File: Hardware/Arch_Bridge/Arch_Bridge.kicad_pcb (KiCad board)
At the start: 2 copper layers, 88.8 x 76 mm, 87 parts, among them J1 Conn_01x02, J3 Conn_01x04, J4 Conn_01x04, Q1 2N3904, Q2 MJE2955, Q3 MJE2955, U1 AP63205WU, U10 74LVC1G04, U11 ESP32-S3-WROOM-1, U12 TXS0102DCT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

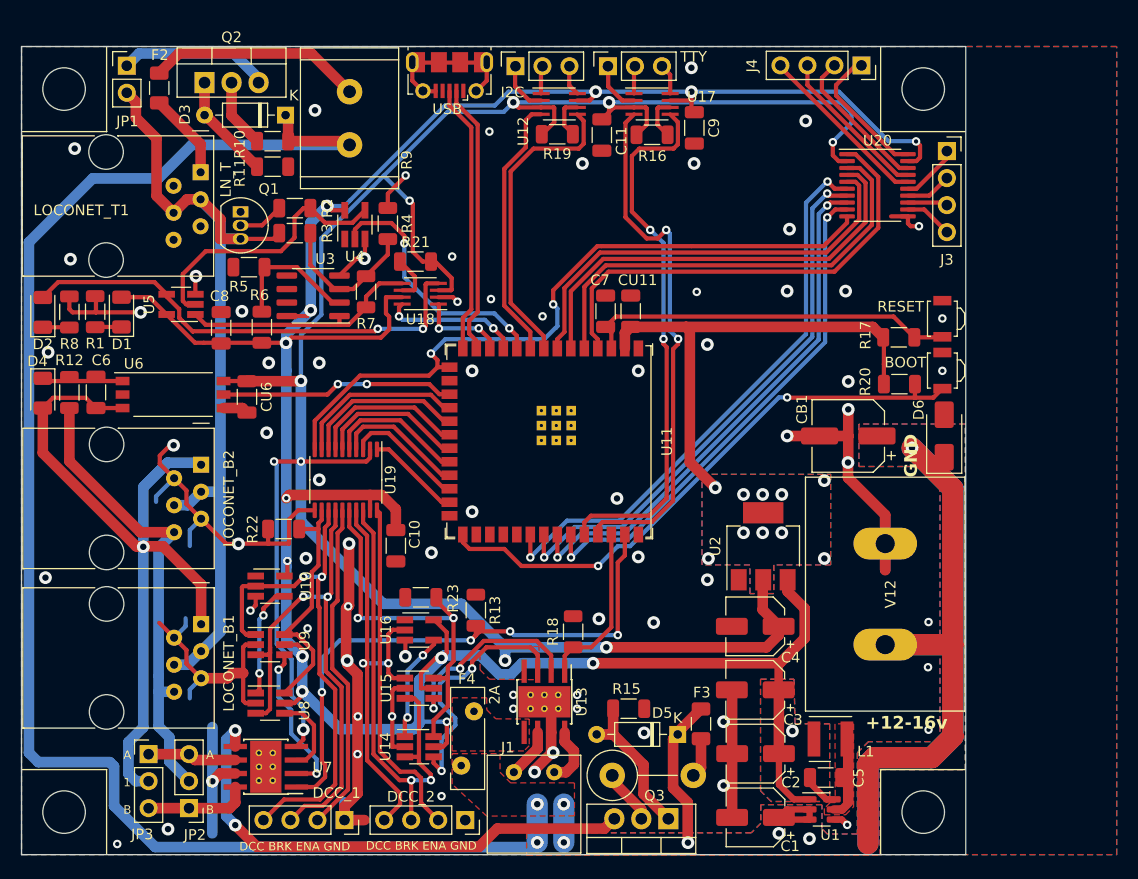
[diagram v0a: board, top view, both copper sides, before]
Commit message: Schematic rev 06 with PCB updates. Needs BOM and Fabs reprocessed.
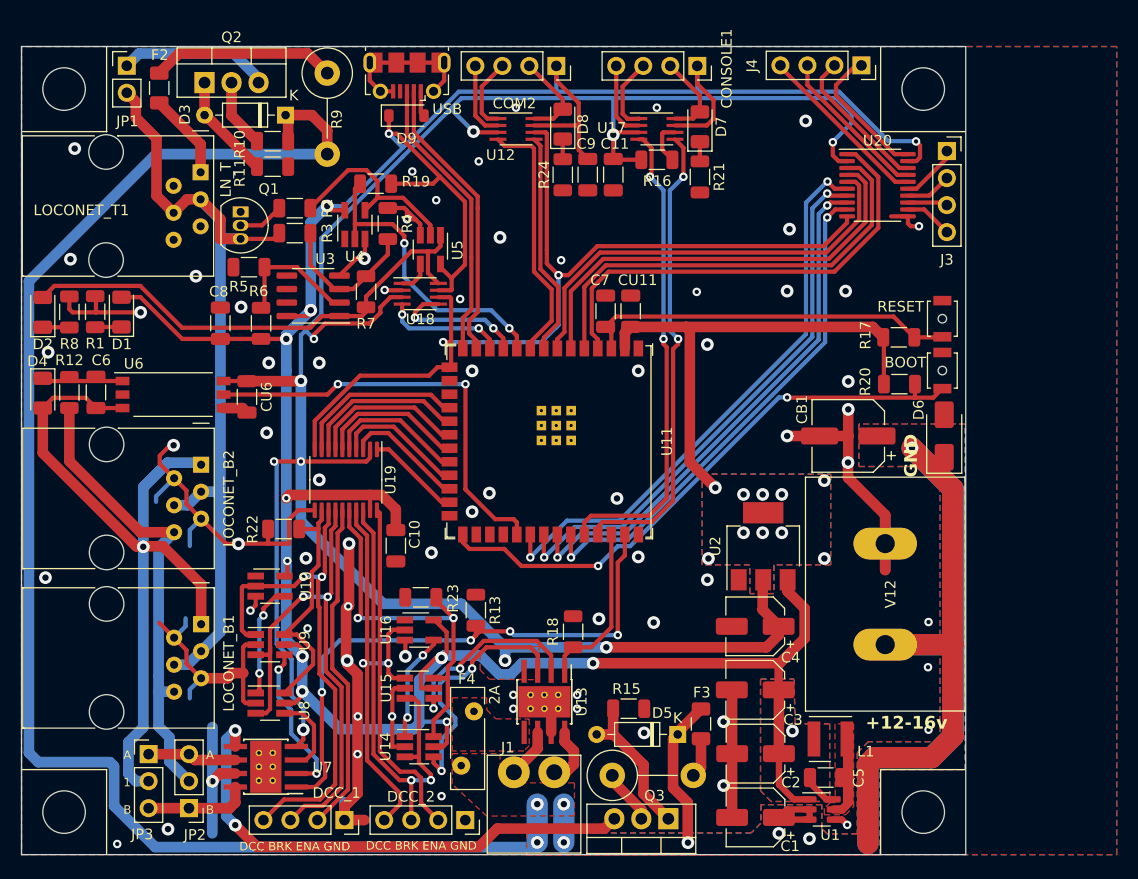
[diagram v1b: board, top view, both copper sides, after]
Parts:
- removed I2C_1, TTY_1: Conn_01x03, Connector_PinSocket_2.54mm:PinSocket_1x03_P2.54mm_Vertical
- added COM2: Conn_01x04, Connector_PinSocket_2.54mm:PinSocket_1x04_P2.54mm_Vertical, F.Cu at (70.3, 21.8)
- added CONSOLE1: Conn_01x03, Connector_PinSocket_2.54mm:PinSocket_1x04_P2.54mm_Vertical, F.Cu at (83.5, 21.8)
- added D7: LED, LED_SMD:LED_1206_3216Metric, F.Cu at (83.8, 27.6)
- added D8: LED, LED_SMD:LED_1206_3216Metric, F.Cu at (70.9, 27.3)
- added D9: PMEG2005EGW, Diode_SMD:D_SOD-123, F.Cu at (56.2, 26.5)
- added R24: 1k, Resistor_SMD:R_1206_3216Metric, F.Cu at (70.9, 32.1)
- BOOT1, RESET1: value B3U-3000P -> B3U-1000P; footprint Button_Switch_SMD:SW_SPST_B3U-3000P -> Button_Switch_SMD:SW_SPST_B3U-1000P-B
- F2: value 500mA -> 250mA
- R11: value 33k -> 3k
- R15: value 3k -> 470
- R21: value 10k -> 1k
- R22, R23: value 10k -> 47k
- R9: value 10 5w -> 33 2w; footprint Resistor_THT:R_Radial_Power_L13.0mm_W9.0mm_P5.00mm -> Resistor_THT:R_Axial_DIN0414_L11.9mm_D4.5mm_P7.62mm_Vertical
- moved R21 27.9 mm to (83.8, 32.3), turned to -90 degrees
- moved U5 24.0 mm to (58.5, 39.1), turned to -90 degrees
- moved R19 17.7 mm to (53.3, 32.9), turned to 0 degrees
- moved C9 10.9 mm to (73.2, 32.0)
- moved R9 7.07 mm to (48.8, 22.5), turned to -90 degrees
- moved U12 4.70 mm to (66.5, 27.8)
- moved USB1 4.00 mm to (56.2, 22.8)
- moved C11 3.88 mm to (75.7, 32.0)
- moved U17 2.39 mm to (79.8, 27.8)
- moved R16 2.39 mm to (79.8, 30.6)
- moved C8 0.43 mm to (38.7, 46.0)
- moved R6 0.37 mm to (42.5, 46.0)
- turned U18 to 0 degrees
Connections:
- R19 pad 1: Net-(U12-OE) -> /LN_TX
- R19 pad 2: +3.3V -> +5V
- R21 pad 1: +3.3V -> Net-(D7-K)
- R21 pad 2: Net-(U18-OE) -> GND
- R7 pad 1: Net-(U18-A1) -> Net-(D2-A)
- R9 pad 1: +12V -> Net-(F2-Pad2)
- R9 pad 2: Net-(F2-Pad2) -> +12V
- U11 pad 17: /RSYNC_IN -> /GPIO9
- U11 pad 31: /GPIO38 -> /RSYNC_IN
- U12 pad 6: Net-(U12-OE) -> /OE
- U17 pad 4: /TXD -> /RXD
- U17 pad 5: /RXD -> /TXD
- U18 pad 1: /LN_COLL -> Net-(U18-B2)
- U18 pad 4: Net-(D2-A) -> /LN_COLL
- U18 pad 5: Net-(U18-A1) -> /LN_RX
- U18 pad 6: Net-(U18-OE) -> /OE
- U18 pad 8: /LN_RX -> Net-(D2-A)
- U3 pad 1: Net-(U18-A1) -> Net-(D2-A)
- U5 pad 1: Net-(U18-A1) -> Net-(D2-A)
- U5 pad 4: Net-(D2-A) -> Net-(U18-B2)
- USB1 pad 1: unconnected-(USB1-VBUS-Pad1) -> Net-(D9-A)
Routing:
- net +5V: track 269.5 -> 306.3 mm, vias 14 -> 13
- net Net-(U18-A1): track 22.9 -> 0.00 mm
- net /OE: track 66.4 -> 87.0 mm
- net /RSYNC_IN: track 22.0 -> 40.3 mm
- net /SDA: track 28.9 -> 21.2 mm
- net Net-(R2-Pad2): track 25.7 -> 18.5 mm
- net /RXD: track 51.3 -> 45.0 mm
- net /TXD: track 49.9 -> 44.2 mm
- net Net-(COM2-Pin_2): track 2.84 -> 8.44 mm
- net Net-(CONSOLE1-Pin_2): track 2.84 -> 8.09 mm
- net Net-(CONSOLE1-Pin_3): track 2.57 -> 7.03 mm
- net Net-(U18-OE): track 4.43 -> 0.00 mm
- net Net-(COM2-Pin_3): track 2.57 -> 6.97 mm
- net /LN_TX: track 24.2 -> 28.5 mm
- net Net-(U12-OE): track 4.02 -> 0.00 mm
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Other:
- board text removed: "Arch Bridge Loconet interface + Railsync"
- board text removed: "I2C"
- board text removed: "TTY"

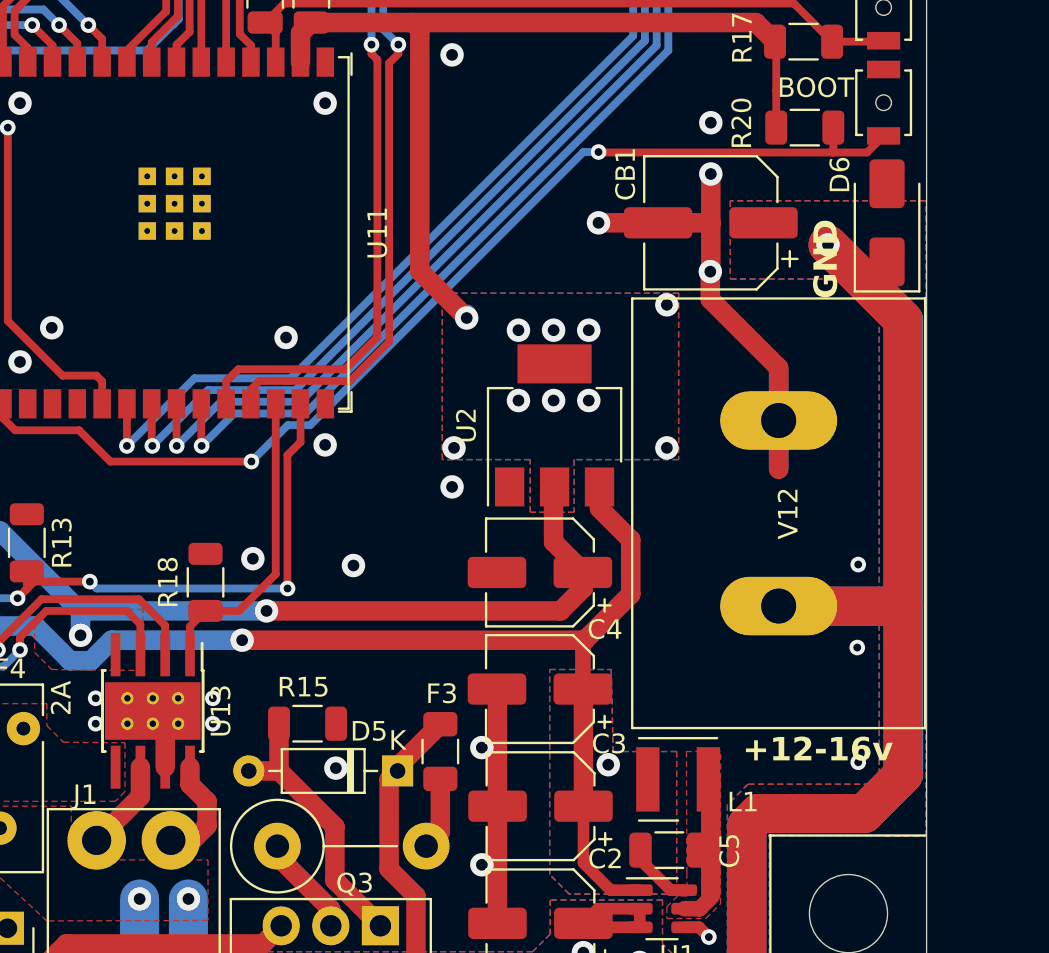
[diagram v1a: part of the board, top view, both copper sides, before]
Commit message: Changed CB1 to through hole for field installaion, no longer in BOM or populated by default.
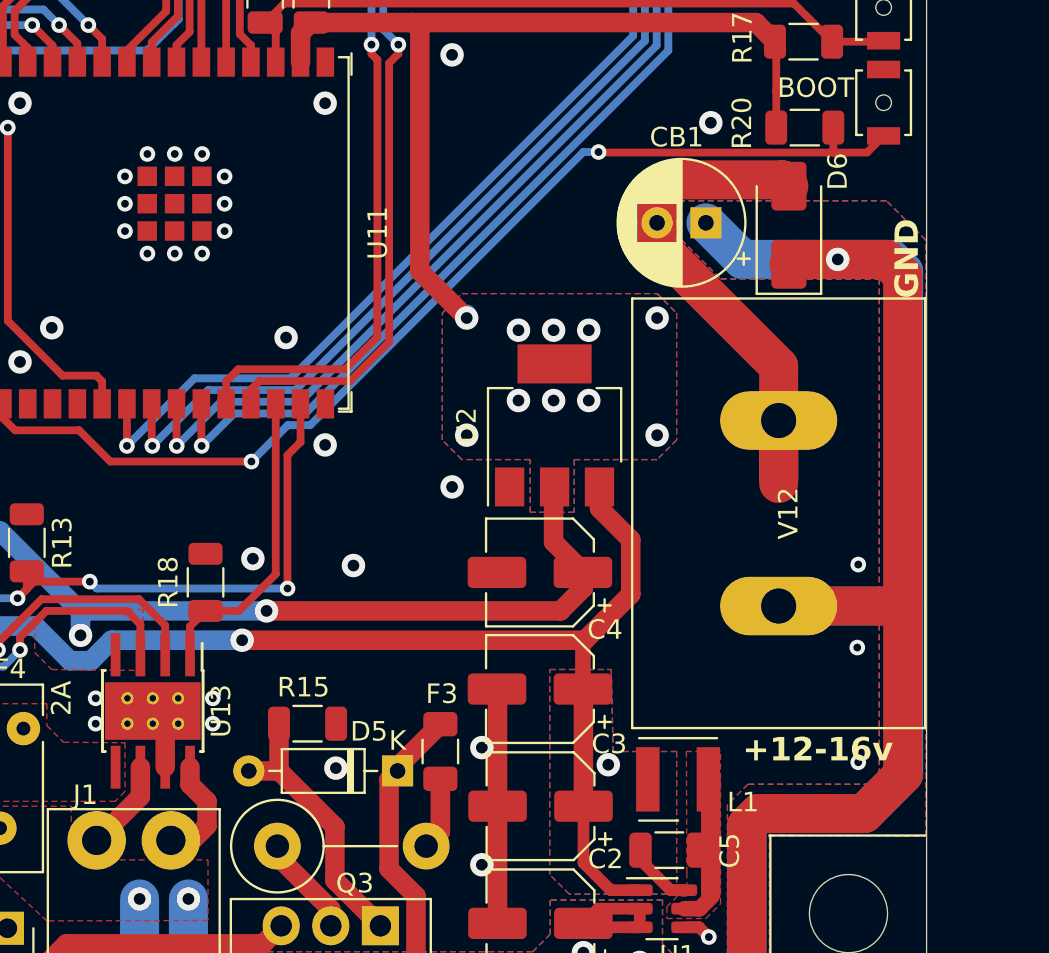
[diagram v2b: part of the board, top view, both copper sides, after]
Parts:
- CB1: footprint Capacitor_SMD:CP_Elec_6.3x7.7 -> Capacitor_THT:CP_Radial_D6.3mm_P2.50mm
- U5: value 74LVC1G02 -> 74xGxx_74AHC1G86
- moved D6 5.03 mm to (101.8, 56.8)
- moved CB1 0.25 mm to (97.5, 56.6)
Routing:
- net +12V: track 272.4 -> 283.7 mm
- net GND: track 209.3 -> 209.5 mm, vias 70 -> 79

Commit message: Added tags for JLCPCB Fabricaton
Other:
- board text added: "+"
- board text added: "-"
- board text added: "JLCJLCJLCJLC"
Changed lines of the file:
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@@
       (net 1 "GND") (pinfunction "GND") (pintype "passive"))
     (pad "41" smd rect (at -2.9 -1.94 90) (size 1 1) (layers "F.Cu" "F.Paste" "F.Mask")
-      (net 1 "GND") (pinfunction "GND") (pintype "passive") (zone_connect 2))
+      (net 1 "GND") (pinfunction "GND") (pintype "passive"))
     (pad "41" smd rect (at -2.9 -0.54 90) (size 1 1) (layers "F.Cu" "F.Paste" "F.Mask")
-      (net 1 "GND") (pinfunction "GND") (pintype "passive") (zone_connect 2))
+      (net 1 "GND") (pinfunction "GND") (pintype "passive"))
     (pad "41" smd rect (at -2.9 0.86 90) (size 1 1) (layers "F.Cu" "F.Paste" "F.Mask")
-      (net 1 "GND") (pinfunction "GND") (pintype "passive") (zone_connect 2))
+      (net 1 "GND") (pinfunction "GND") (pintype "passive"))
     (pad "41" smd rect (at -1.5 -1.94 90) (size 1 1) (layers "F.Cu" "F.Paste" "F.Mask")
-      (net 1 "GND") (pinfunction "GND") (pintype "passive") (zone_connect 2))
+      (net 1 "GND") (pinfunction "GND") (pintype "passive"))
     (pad "41" smd rect (at -1.5 -0.54 90) (size 1 1) (layers "F.Cu" "F.Paste" "F.Mask")
-      (net 1 "GND") (pinfunction "GND") (pintype "passive") (zone_connect 2))
+      (net 1 "GND") (pinfunction "GND") (pintype "passive"))
     (pad "41" smd rect (at -1.5 0.86 90) (size 1 1) (layers "F.Cu" "F.Paste" "F.Mask")
-      (net 1 "GND") (pinfunction "GND") (pintype "passive") (zone_connect 2))
+      (net 1 "GND") (pinfunction "GND") (pintype "passive"))
     (pad "41" smd rect (at -0.1 -1.94 90) (size 1 1) (layers "F.Cu" "F.Paste" "F.Mask")
-      (net 1 "GND") (pinfunction "GND") (pintype "passive") (zone_connect 2))
+      (net 1 "GND") (pinfunction "GND") (pintype "passive"))
     (pad "41" smd rect (at -0.1 -0.54 90) (size 1 1) (layers "F.Cu" "F.Paste" "F.Mask")
-      (net 1 "GND") (pinfunction "GND") (pintype "passive") (zone_connect 2))
+      (net 1 "GND") (pinfunction "GND") (pintype "passive"))
     (pad "41" smd rect (at -0.1 0.86 90) (size 1 1) (layers "F.Cu" "F.Paste" "F.Mask")
-      (net 1 "GND") (pinfunction "GND") (pintype "passive") (zone_connect 2))
+      (net 1 "GND") (pinfunction "GND") (pintype "passive"))
     (model "${ESPRESSIF_3DMODELS}/ESP32-S3-WROOM-1U.STEP"
       (offset (xyz -9 -9.75 0))
@@
   (gr_line (start 108.8 96) (end 108.8 20)
     (stroke (width 0.05) (type default)) (layer "Edge.Cuts"))
+  (gr_text "+" (at 98.5 79) (layer "B.SilkS")
+    (effects (font (size 1 1) (thickness 0.15)) (justify left bottom mirror))
+  )
+  (gr_text "JLCJLCJLCJLC" (at 108.25 66.75 90) (layer "B.SilkS")
+    (effects (font (size 1 1) (thickness 0.15)) (justify left bottom mirror))
+  )
+  (gr_text "-" (at 98.5 69.25) (layer "B.SilkS")
+    (effects (font (size 1 1) (thickness 0.15)) (justify left bottom mirror))
+  )
   (gr_text "Seraphimlabs LLC 2023\ngithub.com/SeraphimlabsLLC" (at 66.95 62.05) (layer "B.SilkS")
     (effects (font (size 1.2 1.2) (thickness 0.15)) (justify bottom mirror))

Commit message: Schematic rev 0.8, PCB update adding current sense filter caps, fixing pull-up on Loconet TX, and slight reposition of U17
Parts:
- added ?: MountingHole_Pad, MountingHole:MountingHole_4.3mm_M4_DIN965_Pad, F.Cu at (104.8, 92.0)
- added C12: 0.015uF, Capacitor_SMD:C_1206_3216Metric_Pad1.33x1.80mm_HandSolder, F.Cu at (71.5, 71.8)
- added C13: 1500pF, Capacitor_SMD:C_1206_3216Metric_Pad1.33x1.80mm_HandSolder, F.Cu at (80.8, 71.8)
- added H1: MountingHole_Pad, MountingHole:MountingHole_4.3mm_M4_DIN965_Pad, F.Cu at (24.0, 24.0)
- added H2: MountingHole_Pad, MountingHole:MountingHole_4.3mm_M4_DIN965_Pad, F.Cu at (104.8, 24.0)
- added H4: MountingHole_Pad, MountingHole:MountingHole_4.3mm_M4_DIN965_Pad, F.Cu at (24.0, 92.0)
- R19: value 10k -> 47k
- U5: value 74xGxx_74AHC1G86 -> 74LVC1G02
- moved R13 15.6 mm to (78.2, 71.7), turned to 90 degrees
- moved R18 3.95 mm to (74.0, 71.7), turned to 90 degrees
- moved C10 2.13 mm to (56.5, 65.2), turned to 0 degrees
- moved JP2 0.92 mm to (34.9, 92.0)
- moved JP3 0.82 mm to (31.2, 87.0)
- moved D9 0.80 mm to (57.0, 26.5)
- moved U7 0.78 mm to (43.2, 87.0)
- moved LOCONET_T1 0.25 mm to (36.8, 32.1)
- moved R22 0.20 mm to (44.5, 65.2)
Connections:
- R19 pad 2: +5V -> +3.3V
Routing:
- net /OUT1_B: track 9.83 -> 0.00 mm
- net +12V: track 283.7 -> 276.1 mm
- net +5V: track 306.3 -> 312.4 mm
- net /LN_DAT: track 80.3 -> 75.5 mm
- net GND: track 209.5 -> 214.2 mm, vias 79 -> 87
- net /OUT1_A: track 8.38 -> 3.88 mm
- net /SNS_2: track 15.7 -> 19.6 mm
- net Net-(Q3-E): track 48.7 -> 52.4 mm
- net /SNS_1: track 54.7 -> 58.4 mm
- net /DCC_1: track 48.4 -> 45.4 mm, vias 2 -> 1
- net /ENA_2o: track 35.5 -> 32.5 mm
- net /BRK_1: track 50.7 -> 53.3 mm, vias 2 -> 1
- net /ENA_1o: track 23.4 -> 25.6 mm, vias 0 -> 3
- net Net-(U7-IN2): track 14.8 -> 16.6 mm, vias 2 -> 0
- net /ENA_2i: track 32.3 -> 33.9 mm, vias 0 -> 1
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- added copper zone on F.Cu, net /OUT1_A
- added copper zone on F.Cu, net /OUT1_B
- added copper zone on B.Cu, net Net-(Q3-E)
- added copper zone on F.Cu, net Net-(Q3-E)
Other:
- outline, holes or cut-outs redrawn

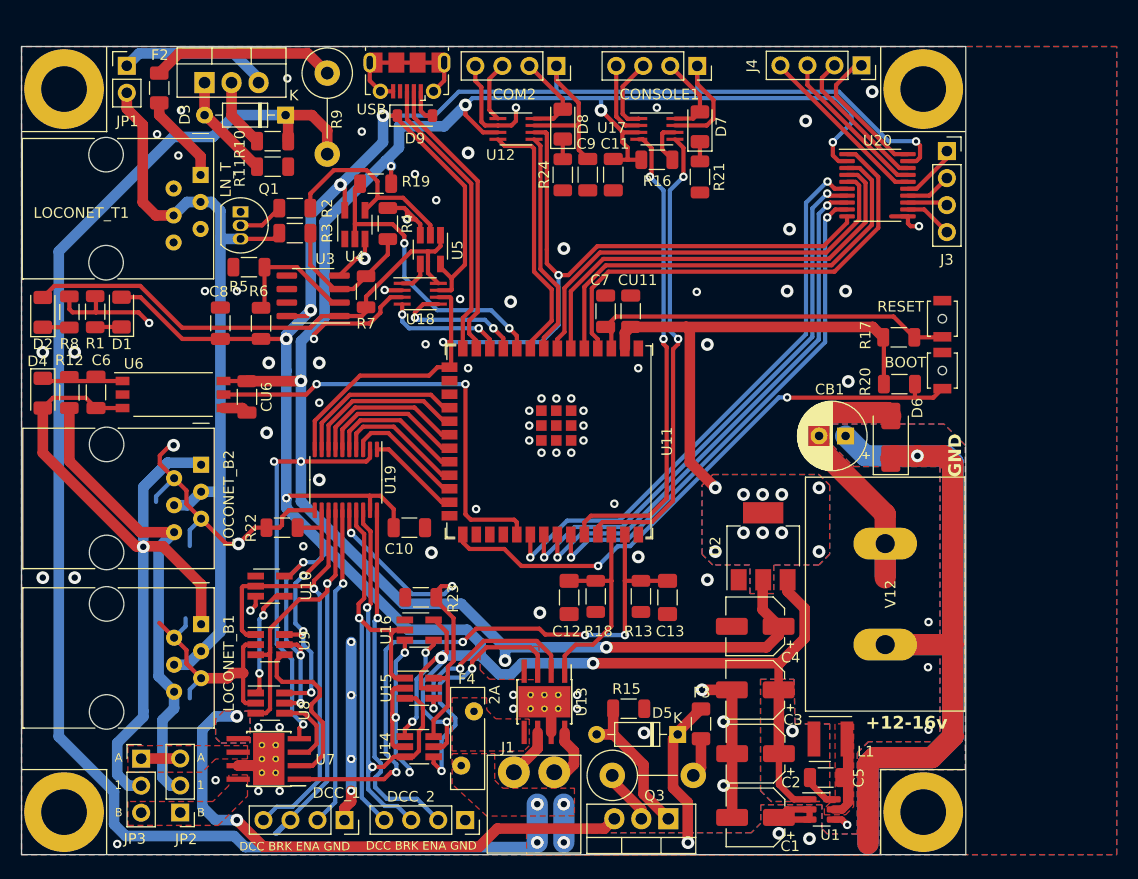
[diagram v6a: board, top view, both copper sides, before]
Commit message: Changed aux track output to use 5.0mm pitch matching EX-8874 track plugs
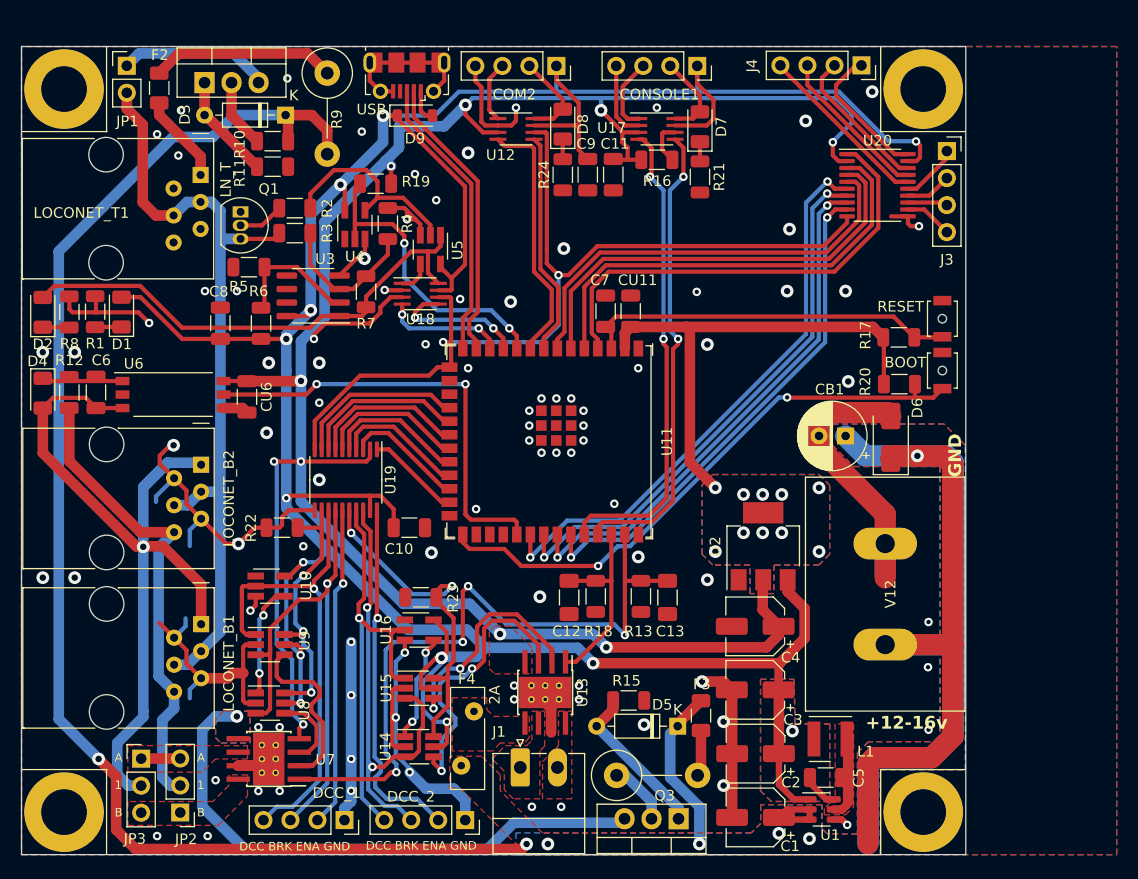
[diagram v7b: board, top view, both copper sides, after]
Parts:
- C12: value 0.015uF -> 15nF
- C13: value 1500pF -> 1.5nF
- J1: footprint Terminal_Wuerth_new:WR-TBL 2P -> Connector_Phoenix_MC:PhoenixContact_MC_1,5_2-G-3.5_1x02_P3.50mm_Horizontal
- moved J1 3.69 mm to (66.9, 87.8)
- moved Q3 0.96 mm to (81.8, 92.6)
- moved U13 0.88 mm to (69.2, 80.8)
- moved F3 0.78 mm to (83.9, 82.9)
- moved R15 0.78 mm to (77.1, 81.5)
- moved D5 0.77 mm to (81.7, 83.9)
- moved R14 0.41 mm to (76.0, 88.5)
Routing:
- net GND: track 214.2 -> 222.7 mm, vias 87 -> 90
- net +12V: track 276.1 -> 269.5 mm, vias 8 -> 7
- net /SNS_1: track 58.4 -> 64.5 mm
- net /OUT2_B: track 5.52 -> 0.00 mm
- net /OUT2_A: track 4.68 -> 0.00 mm
- net /BRK_1: track 53.3 -> 49.5 mm
- net Net-(U13-IN1): track 23.8 -> 27.0 mm
- net Net-(U13-IN2): track 18.4 -> 21.2 mm
- net /SNS_2: track 19.6 -> 18.3 mm
- net +3.3V: track 268.2 -> 266.9 mm
- net Net-(Q3-E): track 52.4 -> 53.6 mm, vias 2 -> 1
- net Net-(D5-A): track 14.1 -> 15.0 mm
- net +5V: track 312.4 -> 311.6 mm
- net Net-(Q3-C): track 5.21 -> 5.93 mm
- net Net-(F3-Pad1): track 3.75 -> 4.35 mm
- added copper zone on F.Cu, net /OUT2_A
- added copper zone on F.Cu, net /OUT2_B
